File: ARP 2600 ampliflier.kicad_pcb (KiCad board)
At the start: 2 copper layers, 88 x 81 mm, 44 parts, among them P1 CONN_01X04, P2 CONN_01X04, P3 CONN_01X04, P4 CONN_01X04, Q1 2N3904, U1 TDA7269A, U2 LM7812CT, U3 LM7912CT

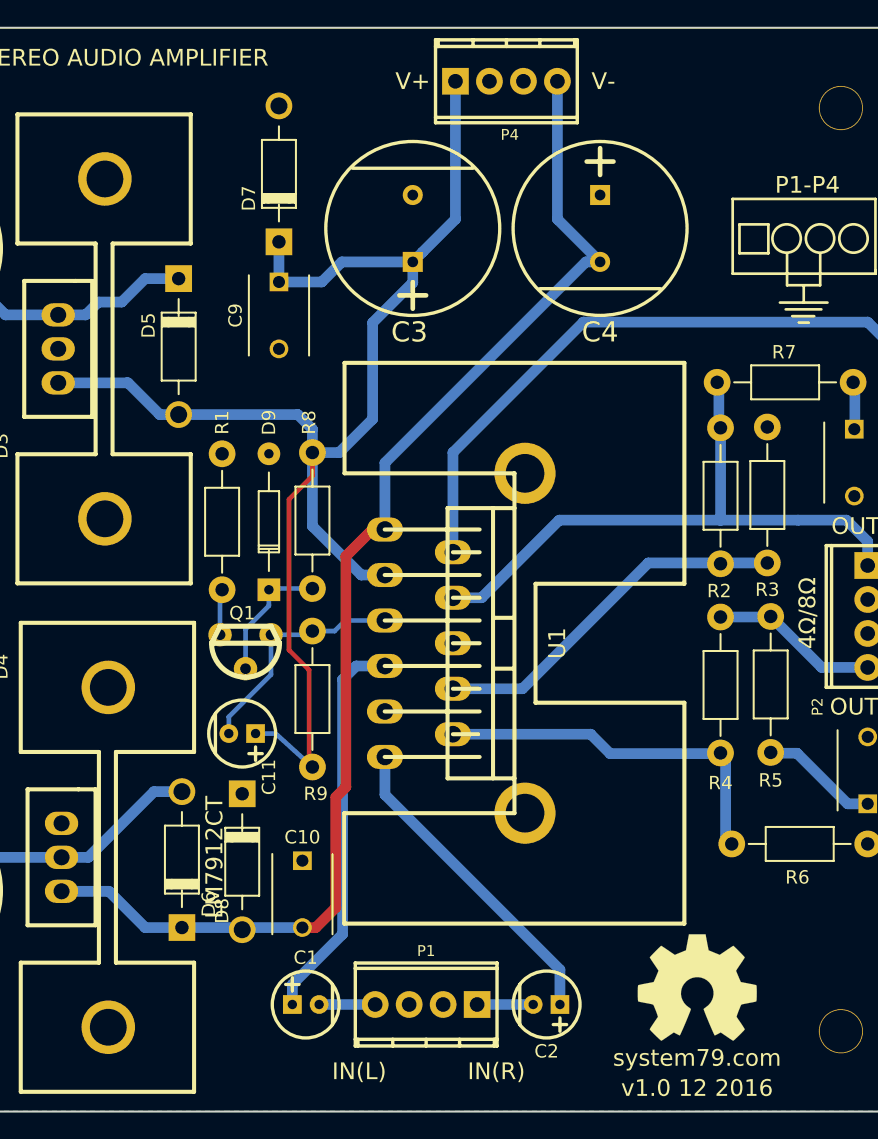
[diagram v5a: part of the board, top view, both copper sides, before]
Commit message: fixed another mistake - two -Vs pins on amplifier you donut
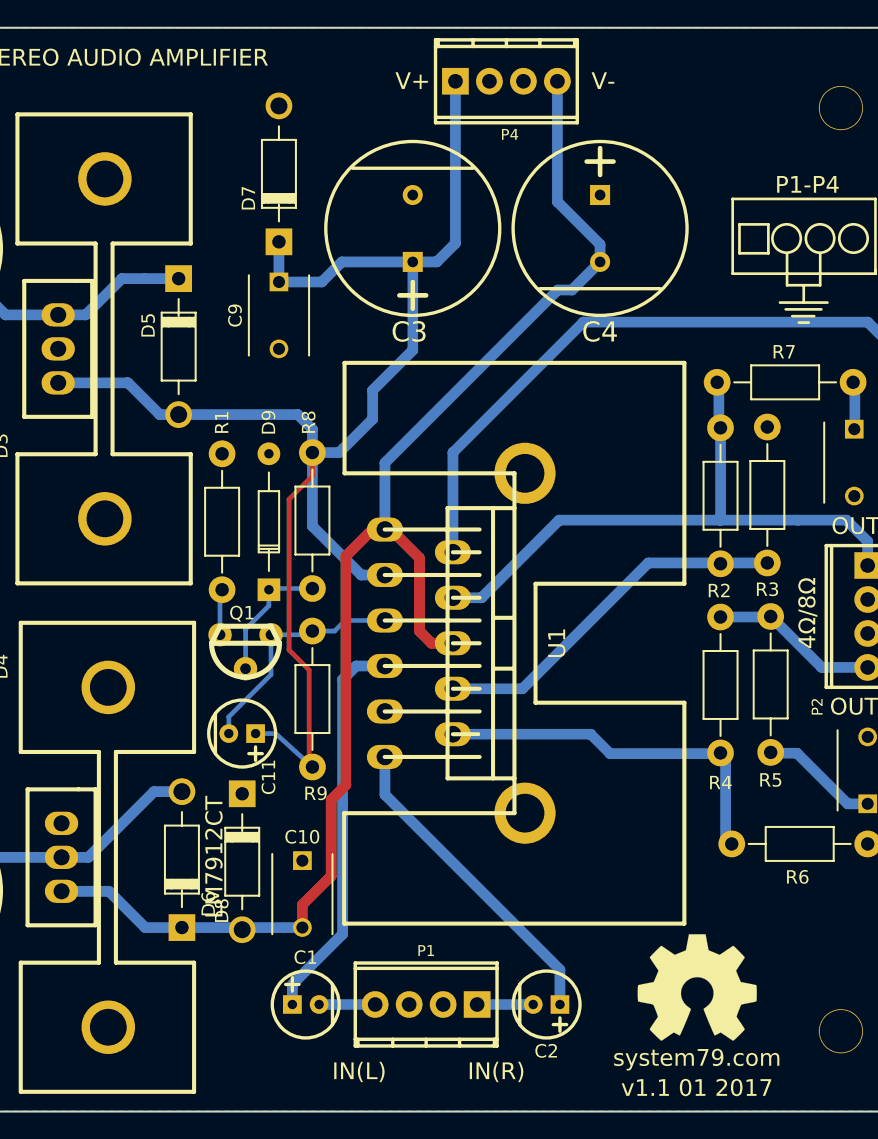
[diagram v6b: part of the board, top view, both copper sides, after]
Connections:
- U1 pad 6: (no net) -> -V
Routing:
- net -V: track 94.8 -> 106.0 mm
- net +V: track 112.4 -> 113.5 mm
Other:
- board text added: "v1.1 01 2017"
- board text removed: "v1.0 12 2016"
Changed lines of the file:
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@@
 (kicad_pcb (version 4) (host pcbnew 4.0.2-stable)
   (general
-    (links 77)
+    (links 78)
     (no_connects 0)
     (area 93.924999 70.924999 182.075001 152.075001)
     (thickness 1.6)
     (drawings 44)
-    (tracks 156)
+    (tracks 163)
     (zones 0)
     (modules 44)
@@
       (effects (font (size 1 1) (thickness 0.15)))
     )
-    (fp_text value 18K (at 5.08 3.81 90) (layer F.Fab)
+    (fp_text value 18K (at 5.185 0.005 90) (layer F.Fab)
       (effects (font (size 1 1) (thickness 0.15)))
     )
@@
       (effects (font (size 1 1) (thickness 0.15)))
     )
-    (fp_text value 4.7 (at 5.08 3.81 270) (layer F.Fab)
+    (fp_text value 4.7 (at 5.015 -0.065 270) (layer F.Fab)
       (effects (font (size 1 1) (thickness 0.15)))
     )
@@
       (effects (font (size 1 1) (thickness 0.15)))
     )
-    (fp_text value 4.7 (at 5.08 3.81) (layer F.Fab)
+    (fp_text value 4.7 (at 5.335 0.29) (layer F.Fab)
       (effects (font (size 1 1) (thickness 0.15)))
     )
@@
     (pad 5 thru_hole oval (at -1.69926 5.08 270) (size 1.80086 2.70002) (drill 1.24968) (layers *.Cu *.Mask F.SilkS)
       (net 16 "Net-(C11-Pad2)"))
-    (pad 6 thru_hole oval (at 0 0 270) (size 1.80086 2.70002) (drill 1.24968) (layers *.Cu *.Mask F.SilkS))
+    (pad 6 thru_hole oval (at 0 0 270) (size 1.80086 2.70002) (drill 1.24968) (layers *.Cu *.Mask F.SilkS)
+      (net 7 -V))
     (pad 7 thru_hole oval (at 1.69926 5.08 270) (size 1.80086 2.70002) (drill 1.24968) (layers *.Cu *.Mask F.SilkS)
       (net 1 "Net-(C1-Pad1)"))
@@
     (effects (font (size 1.25 1.25) (thickness 0.25)))
   )
-  (gr_text "v1.0 12 2016" (at 165.25 150.25) (layer F.SilkS)
+  (gr_text "v1.1 01 2017" (at 165.25 150.25) (layer F.SilkS)
     (effects (font (size 1.25 1.25) (thickness 0.25)))
   )
@@
   (segment (start 155 141.4) (end 155 144) (width 0.8) (layer B.Cu) (net 3))
   (segment (start 148.81 144) (end 153 144) (width 0.8) (layer B.Cu) (net 4))
+  (segment (start 144 88.5) (end 144 95.1) (width 0.8) (layer B.Cu) (net 6))
+  (segment (start 144 95.1) (end 141 98.1) (width 0.8) (layer B.Cu) (net 6))
+  (segment (start 141 98.1) (end 141 100.25) (width 0.8) (layer B.Cu) (net 6))
+  (segment (start 141 100.25) (end 138.5 102.75) (width 0.8) (layer B.Cu) (net 6))
+  (segment (start 138.5 102.75) (end 136.5 102.75) (width 0.8) (layer B.Cu) (net 6))
+  (segment (start 147.19 75) (end 147.19 87.11) (width 0.8) (layer B.Cu) (net 6))
+  (segment (start 147.19 87.11) (end 145.8 88.5) (width 0.8) (layer B.Cu) (net 6))
+  (segment (start 145.8 88.5) (end 145.7 88.5) (width 0.8) (layer B.Cu) (net 6))
+  (segment (start 145.7 88.5) (end 144 88.5) (width 0.8) (layer B.Cu) (net 6))
   (segment (start 126.50254 99.91) (end 135.41 99.91) (width 0.8) (layer B.Cu) (net 6))
   (segment (start 135.41 99.91) (end 136.5 101) (width 0.8) (layer B.Cu) (net 6))
   (segment (start 136.5 101) (end 136.5 102.75) (width 0.8) (layer B.Cu) (net 6))
-  (segment (start 144 88.5) (end 144 90.05) (width 0.8) (layer B.Cu) (net 6))
-  (segment (start 144 90.05) (end 141 93.05) (width 0.8) (layer B.Cu) (net 6))
-  (segment (start 141 93.05) (end 141 100.25) (width 0.8) (layer B.Cu) (net 6))
-  (segment (start 141 100.25) (end 138.5 102.75) (width 0.8) (layer B.Cu) (net 6))
-  (segment (start 138.5 102.75) (end 136.5 102.75) (width 0.8) (layer B.Cu) (net 6))
   (segment (start 126.50254 99.91) (end 125.089048 99.91) (width 0.8) (layer B.Cu) (net 6))
   (segment (start 125.089048 99.91) (end 122.719048 97.54) (width 0.8) (layer B.Cu) (net 6))
@@
   (segment (start 133.84 89.84) (end 134 90) (width 0.8) (layer B.Cu) (net 6))
   (segment (start 133.99746 89.99746) (end 134 90) (width 0.8) (layer B.Cu) (net 6))
-  (segment (start 147.19 85.31) (end 144.749999 87.750001) (width 0.8) (layer B.Cu) (net 6))
-  (segment (start 144.749999 87.750001) (end 144 88.5) (width 0.8) (layer B.Cu) (net 6))
   (segment (start 141.92 111.89968) (end 142.36958 111.89968) (width 0.8) (layer B.Cu) (net 6))
-  (segment (start 147.19 75) (end 147.19 85.31) (width 0.8) (layer B.Cu) (net 6))
-  (segment (start 135.75 138.25) (end 136.75 138.25) (width 0.8) (layer F.Cu) (net 7))
-  (segment (start 136.75 138.25) (end 138.25 136.75) (width 0.8) (layer F.Cu) (net 7))
-  (segment (start 138.25 136.75) (end 138.25 128.5) (width 0.8) (layer F.Cu) (net 7))
+  (segment (start 135.75 138.25) (end 135.75 136.55) (width 0.8) (layer F.Cu) (net 7))
+  (segment (start 135.75 136.55) (end 137.9 134.4) (width 0.8) (layer F.Cu) (net 7))
+  (segment (start 137.9 134.4) (end 137.9 128.7) (width 0.8) (layer F.Cu) (net 7))
+  (segment (start 140.99884 108.50116) (end 141.92 108.50116) (width 0.8) (layer F.Cu) (net 7))
+  (segment (start 137.9 128.7) (end 139 127.6) (width 0.8) (layer F.Cu) (net 7))
+  (segment (start 139 127.6) (end 139 110.5) (width 0.8) (layer F.Cu) (net 7))
   (segment (start 139 110.5) (end 140.99884 108.50116) (width 0.8) (layer F.Cu) (net 7))
-  (segment (start 138.25 128.5) (end 139 127.75) (width 0.8) (layer F.Cu) (net 7))
-  (segment (start 139 127.75) (end 139 110.5) (width 0.8) (layer F.Cu) (net 7))
-  (segment (start 140.99884 108.50116) (end 141.92 108.50116) (width 0.8) (layer F.Cu) (net 7))
-  (segment (start 158 88.5) (end 156.93934 88.5) (width 0.8) (layer B.Cu) (net 7))
-  (segment (start 156.93934 88.5) (end 141.92 103.51934) (width 0.8) (layer B.Cu) (net 7))
+  (segment (start 154.81 75) (end 154.81 84.01) (width 0.8) (layer B.Cu) (net 7))
+  (segment (start 154.81 84.01) (end 158 87.2) (width 0.8) (layer B.Cu) (net 7))
+  (segment (start 158 87.2) (end 158 88.5) (width 0.8) (layer B.Cu) (net 7))
+  (segment (start 158 88.5) (end 155.9 90.6) (width 0.8) (layer B.Cu) (net 7))
+  (segment (start 155.9 90.6) (end 154.83934 90.6) (width 0.8) (layer B.Cu) (net 7))
+  (segment (start 154.83934 90.6) (end 141.92 103.51934) (width 0.8) (layer B.Cu) (net 7))
   (segment (start 141.92 103.51934) (end 141.92 108.50116) (width 0.8) (layer B.Cu) (net 7))
+  (segment (start 147 117) (end 145.4 117) (width 0.8) (layer F.Cu) (net 7))
+  (segment (start 145.4 117) (end 144.5 116.1) (width 0.8) (layer F.Cu) (net 7))
+  (segment (start 144.5 116.1) (end 144.5 110.63158) (width 0.8) (layer F.Cu) (net 7))
+  (segment (start 144.5 110.63158) (end 142.36958 108.50116) (width 0.8) (layer F.Cu) (net 7))
+  (segment (start 142.36958 108.50116) (end 141.92 108.50116) (width 0.8) (layer F.Cu) (net 7))
   (segment (start 126.74746 138.25) (end 124 138.25) (width 0.8) (layer B.Cu) (net 7))
   (segment (start 124 138.25) (end 121.29 135.54) (width 0.8) (layer B.Cu) (net 7))
@@
   (segment (start 126.74746 138.25) (end 131.09254 138.25) (width 0.8) (layer B.Cu) (net 7))
   (segment (start 131.09254 138.25) (end 131.25254 138.41) (width 0.8) (layer B.Cu) (net 7))
-  (segment (start 154.81 75) (end 154.81 85.31) (width 0.8) (layer B.Cu) (net 7))
-  (segment (start 154.81 85.31) (end 158 88.5) (width 0.8) (layer B.Cu) (net 7))
   (segment (start 178 129) (end 176.5 129) (width 0.8) (layer B.Cu) (net 8))
   (segment (start 176.5 129) (end 172.722 125.222) (width 0.8) (layer B.Cu) (net 8))
@@
   (segment (start 136.5 112.91) (end 133.33694 112.91) (width 0.35) (layer B.Cu) (net 17) (status 10))
   (segment (start 133.33694 112.91) (end 133.24746 112.99948) (width 0.35) (layer B.Cu) (net 17))
-  (segment (start 122.25 91.5) (end 124 89.75) (width 0.8) (layer B.Cu) (net 18))
+  (segment (start 117.5 92.46) (end 119.54968 92.46) (width 0.8) (layer B.Cu) (net 18))
+  (segment (start 119.54968 92.46) (end 122.25968 89.75) (width 0.8) (layer B.Cu) (net 18))
+  (segment (start 122.25968 89.75) (end 124 89.75) (width 0.8) (layer B.Cu) (net 18))
   (segment (start 124 89.75) (end 126.50254 89.75) (width 0.8) (layer B.Cu) (net 18))
-  (segment (start 120.50968 91.5) (end 122.25 91.5) (width 0.8) (layer B.Cu) (net 18))
-  (segment (start 117.5 92.46) (end 119.54968 92.46) (width 0.8) (layer B.Cu) (net 18))
-  (segment (start 119.54968 92.46) (end 120.50968 91.5) (width 0.8) (layer B.Cu) (net 18))
   (segment (start 111.1 90) (end 113.56 92.46) (width 0.8) (layer B.Cu) (net 18))
   (segment (start 113.56 92.46) (end 117.5 92.46) (width 0.8) (layer B.Cu) (net 18))
